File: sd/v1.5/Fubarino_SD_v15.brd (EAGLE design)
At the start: 71.1 x 25.4 mm, 33 parts, among them IC1 PIC32MX440F256H-80I/PT, IC2 MCP1702T-3302E/MB, J1 MICRO_SD_CARD_SOCKET, J2 M28USEPIN1, J3 M28NOPIN1, J8 UX60A-MB-5ST, Q1 8MHz, Q2 32.768 KHz

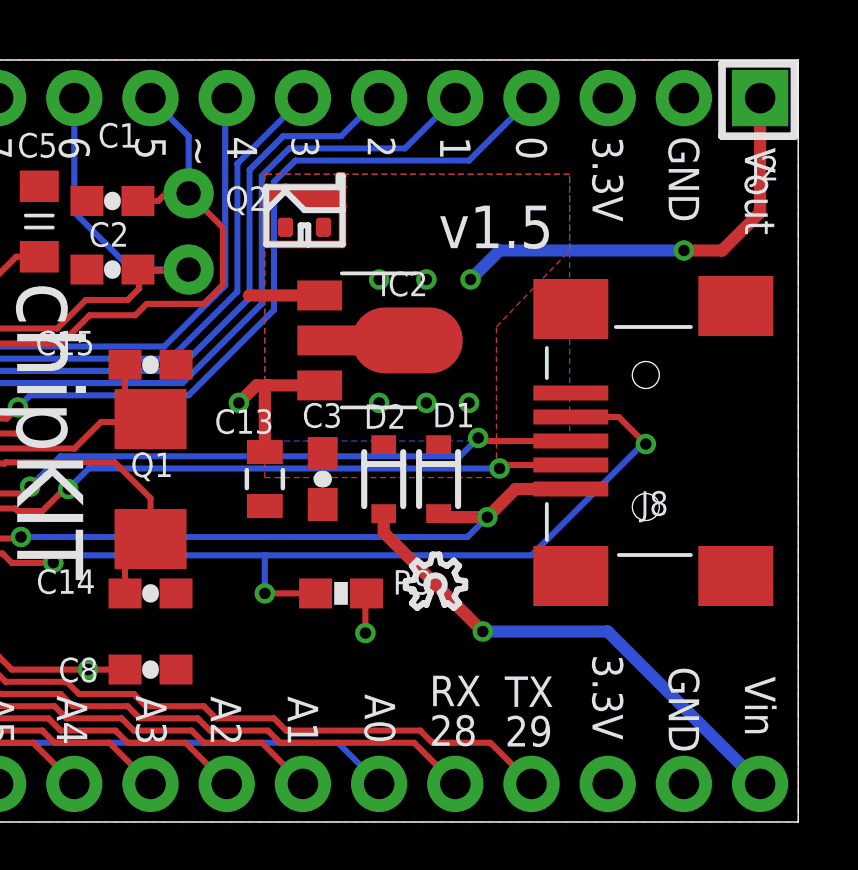
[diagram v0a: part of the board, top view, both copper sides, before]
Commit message: Added Rick's QR code to top silk layer. Still v1.5
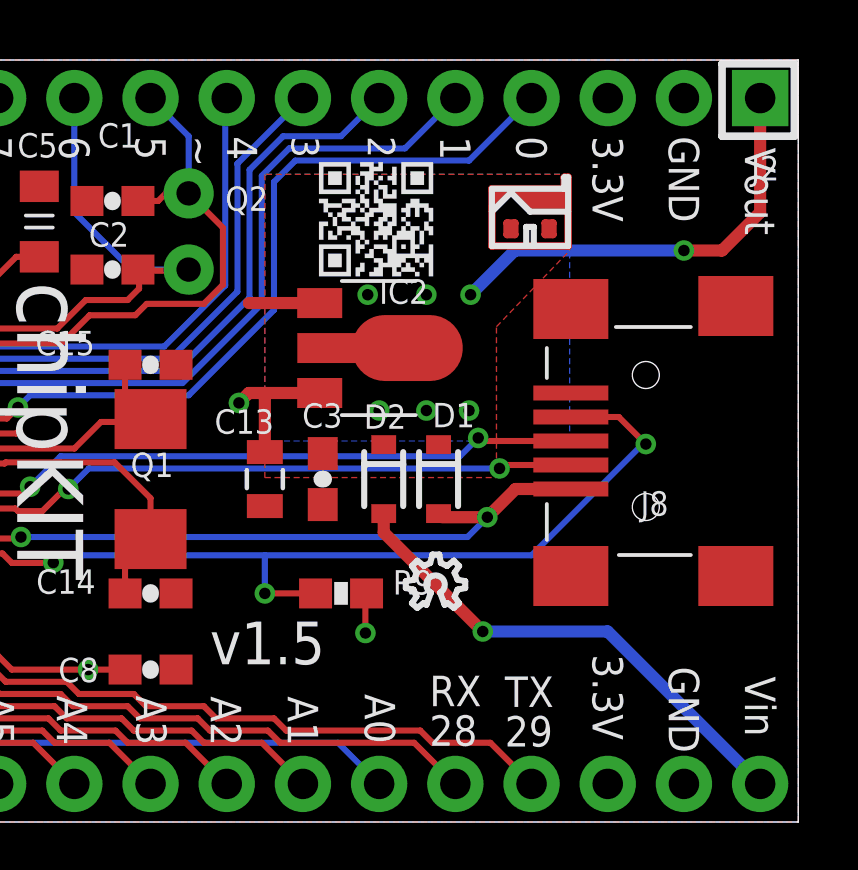
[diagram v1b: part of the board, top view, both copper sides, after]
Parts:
- moved U$1 7.52 mm to (62.2, 19.2)
- moved IC2 0.25 mm to (57.1, 15.8)

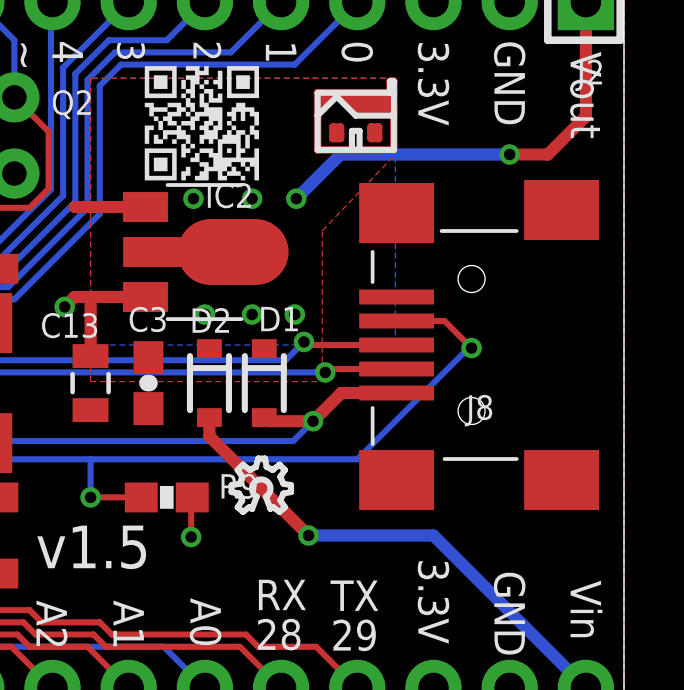
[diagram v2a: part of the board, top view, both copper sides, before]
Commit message: Swapped USB connector for Microchip's Hirose.
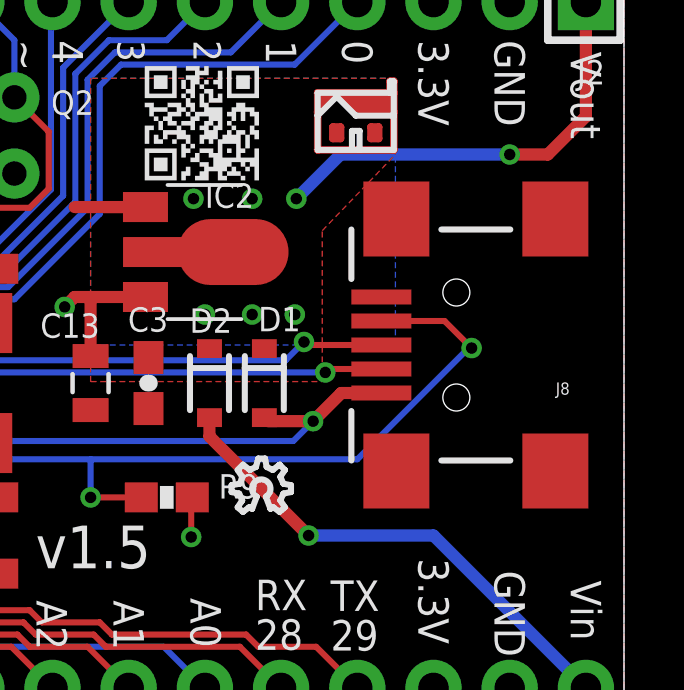
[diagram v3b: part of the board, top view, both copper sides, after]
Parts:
- J8: value UX60A-MB-5ST -> USB-5PIN; device SparkFun02-20-08:USB-MINIB -> SchmalzHaus:USB-MINIB-5PIN-HIROSE-UX60-MB-5ST
- moved J8 0.51 mm to (65.5, 12.7), turned to 90 degrees
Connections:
- net GND: now also J8.MTN1, J8.MTN2, J8.MTN3, J8.MTN4; no longer J8.G1, J8.G2, J8.G3, J8.G4
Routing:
- net D+: track 20.6 -> 20.0 mm
- net VBUS: track 22.1 -> 21.6 mm
- net USBID: track 29.8 -> 30.4 mm
- net D-: track 20.4 -> 19.9 mm

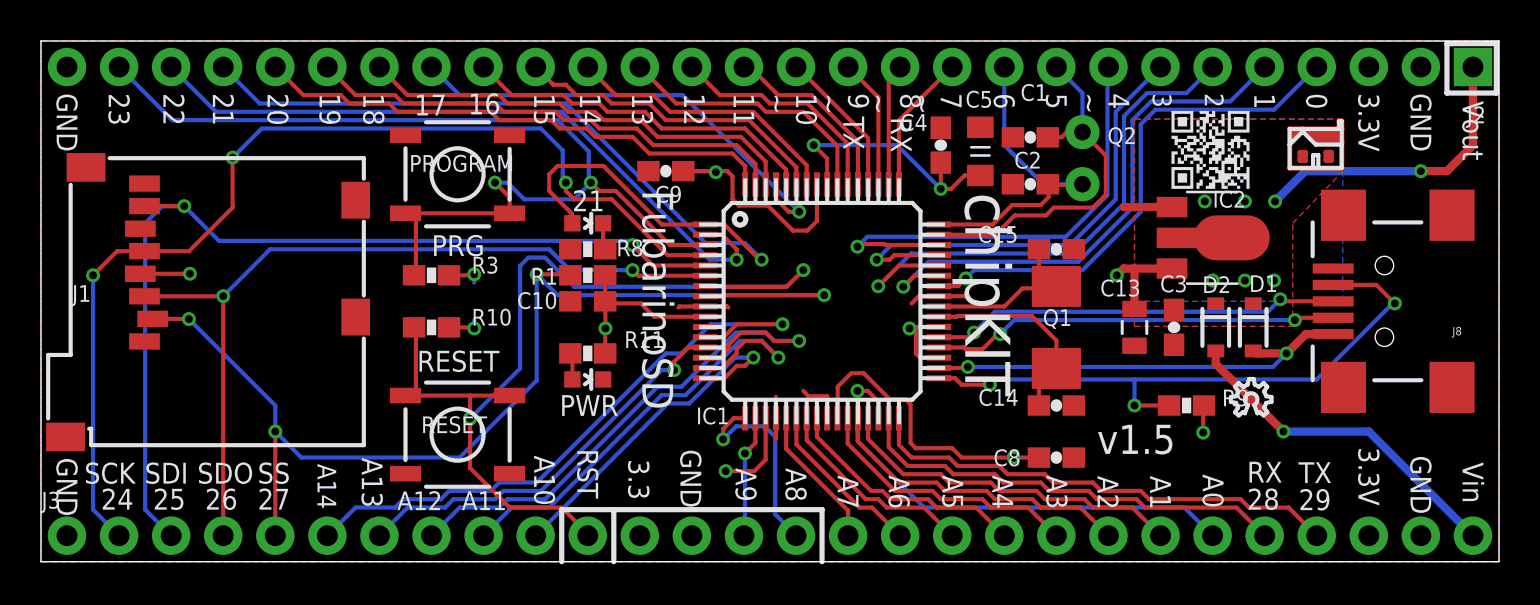
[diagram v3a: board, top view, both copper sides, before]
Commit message: Updated Fubarino SD v1.5 board with CE, RoHS, chipKIT on silk, updated BOM, rendered top and bottom from gerbers.
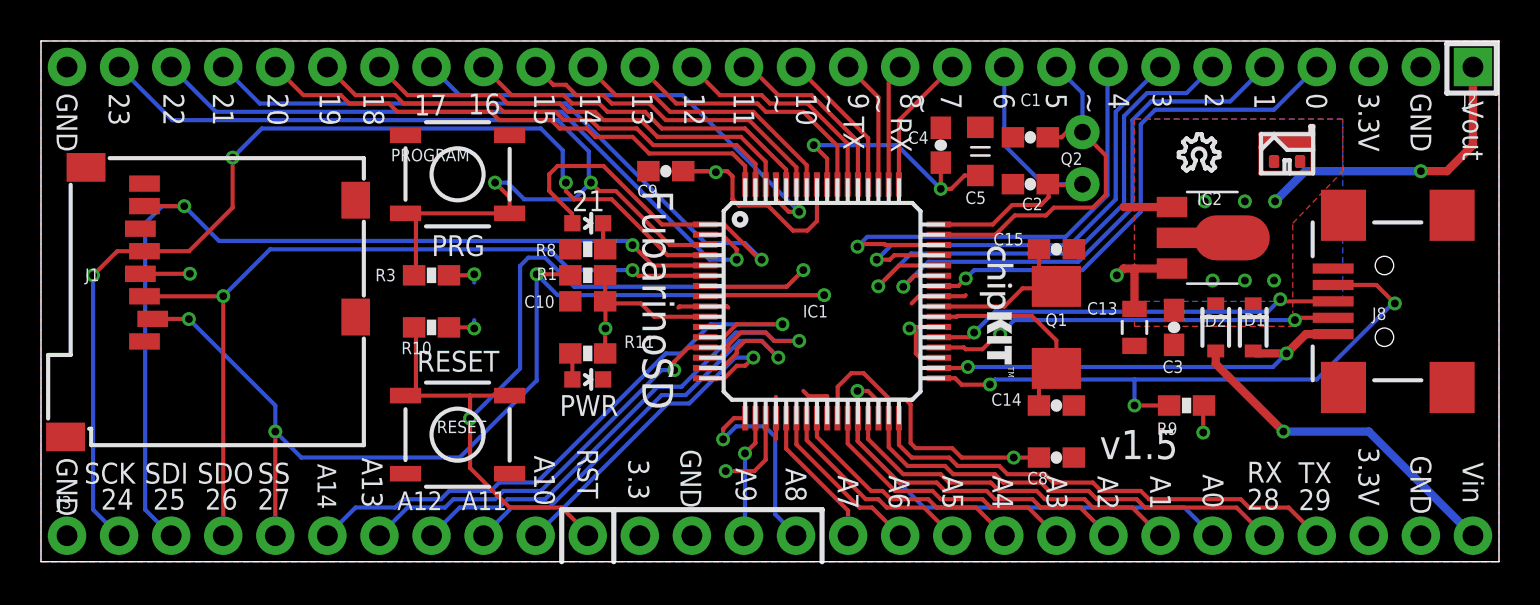
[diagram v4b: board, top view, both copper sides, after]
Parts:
- added DRILEGEND: (no value), drilegend:DRILEGEND
- added U$2: CE_MARK5MM, SchmalzHausPublic:CE_5MM
- added U$3: ROHS_GARBAGE, SchmalzHausPublic:ROHS_GARBAGE_5MM
- added U$4, U$5: CHIPKIT2MM, SchmalzHausPublic:CHIPKIT_2MM
- moved LOGO1 12.2 mm to (55.5, 19.1)
- moved U$1 1.42 mm to (60.8, 18.9)
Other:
- board text added: "01-16"
- board text added: "01-20"
- board text added: "ASSEMBLY NOTES: UNLESS OTHERWISE SPECIFIED 1. ALL COMONENTS ARE RoHS COMPLIANT. 2. ALL THROUGH HOLE COMPONENTS MOUNTED ON THE TOP SIDE 3. ALL COMPONENTS AHLL BE MOUNTED FLUSH TO THE BOARD 4. ALL UNUSED COMPONENTS PADS SHALL BE FREE OF SOLDER 5. ALL LEADS SHALL BE TRIMMED TO A MAXIMUM LENGTH OF : N/A 6. MAXIMUM COMPONENT HEIGHT NOT TO EXEED: N/A 7. THESE COMPONENTS REQUIRE SOCKETS: NONE. 8. UNPOPU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"
- board text added: "Fubarino SD"
- board text added: "LAYER-STACK"
- board text added: "Notes: This PCB to be manufactued to meet all acceptance levels of a CLASS 2 PCB per ANSI/IPC-A-600G. Material: Isola PCL370HR FR-4 or equivalent. Multilayer 2 Layers Controlled Impedance Cu weight external layers : 1oz Cu weight internal layers : Finished overall thickenss : 0.062 Finish: Immersion Gold X Immersion Tin Soldermask over bare copper (SMOBC) with Hot-Air-Leveled-Solder If edge conne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"
- board text added: "TITLE: FUBARINO SD VERSION: 1.5 DATE: 2/26/2013 PCB DESIGNER: BRIAN SCHMALZ ENGINEER: BRIAN SCHMALZ"
- board text removed: "chipKIT"
